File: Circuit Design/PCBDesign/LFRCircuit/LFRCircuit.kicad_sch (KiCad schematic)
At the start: 13 parts, among them M1 Motor_DC, M2 Motor_DC, U1 L293D

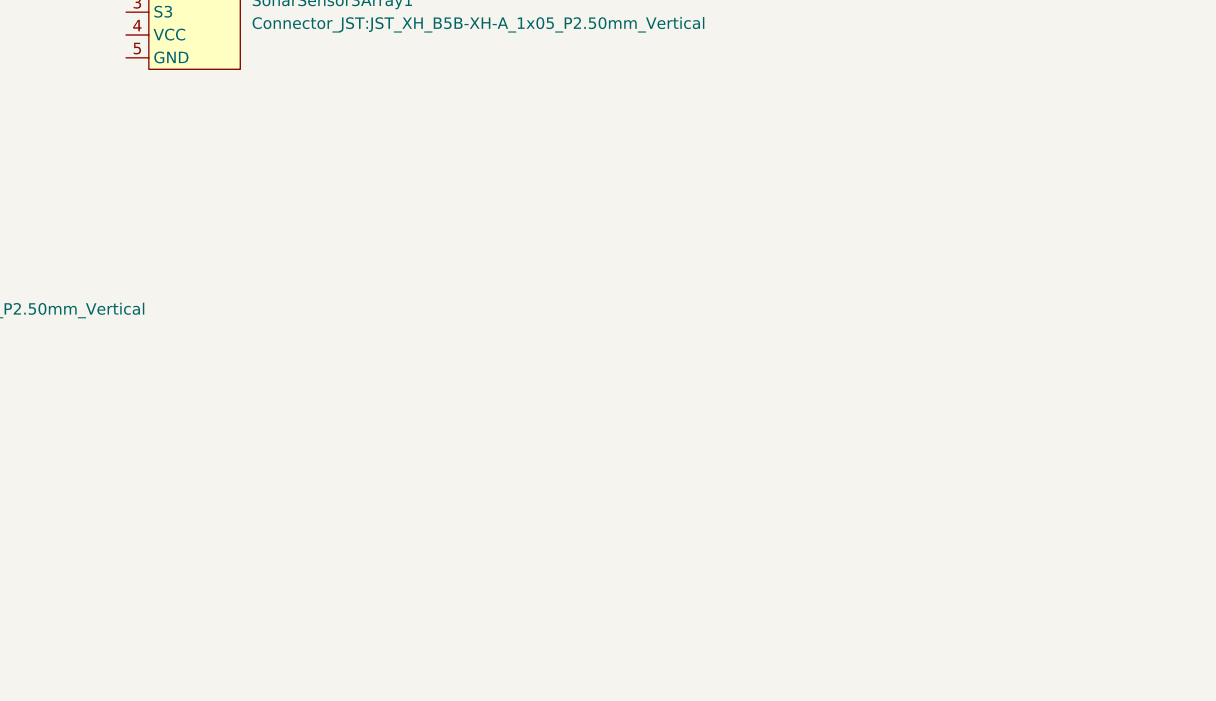
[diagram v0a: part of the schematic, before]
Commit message: Added Rotary Encoder and OLED Display Schematic
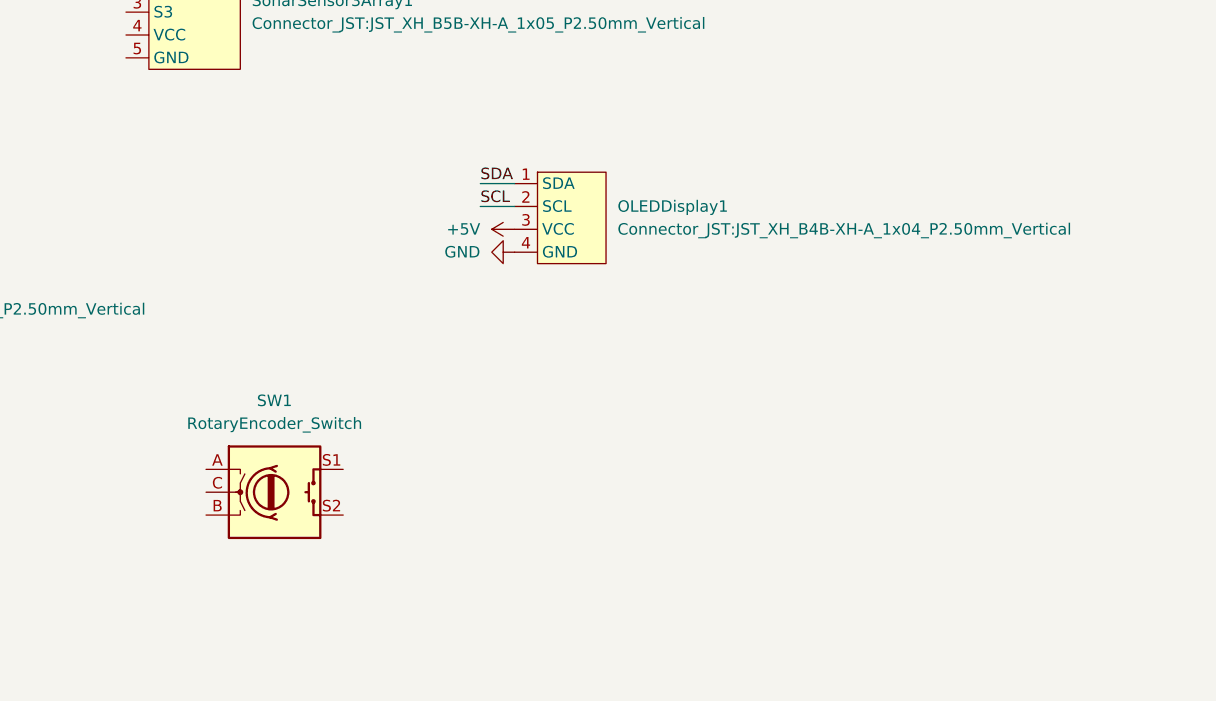
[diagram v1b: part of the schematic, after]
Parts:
- added OLEDDisplay1: ~, Connector_JST:JST_XH_B4B-XH-A_1x04_P2.50mm_Vertical, symbol LFRSymbolLib:SH1106_OLEDDisplay
- added SW1: RotaryEncoder_Switch, symbol Device:RotaryEncoder_Switch
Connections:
- net +5V: now also OLEDDisplay1.3 (VCC)
- net GND: now also OLEDDisplay1.4 (GND)
- net SCL: now also OLEDDisplay1.2 (SCL)
- net SDA: now also OLEDDisplay1.1 (SDA)

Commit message: Finalized the Schematics
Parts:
- removed SW1: RotaryEncoder_Switch, symbol Device:RotaryEncoder_Switch
- added BMSModule1: ~, Connector_JST:JST_XH_B2B-XH-A_1x02_P2.50mm_Vertical, symbol LFRSymbolLib:BMSModule
- added C3: 10uF, symbol Device:C
- added C4, C5: 0.1uF, symbol Device:C
- added C6, C7: 22uF, symbol Device:C
- added C8: 75pF, symbol Device:C
- added D5: D, symbol Device:D
- added L1: 15uH, symbol Device:L
- added R1: 49.9, symbol Device:R
- added R2: 100K, symbol Device:R
- added R3: 13.3K, symbol Device:R
- added R4: 511K, symbol Device:R
- added R5: 105K, symbol Device:R
- added RotaryEncoder1: ~, Connector_JST:JST_XH_B5B-XH-A_1x05_P2.50mm_Vertical, symbol LFRSymbolLib:RotaryEncoder
- added U2: TPS54202DDC, Package_TO_SOT_SMD:SOT-23-6, symbol Regulator_Switching:TPS54202DDC
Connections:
- net +12V: now also BMSModule1.1 (12V), C3.1, C4.1, D5.2 (A), R4.1, U2.3 (VIN)
- net +5V: now also INA1.8 (VCC), SonarSensor3Array1.4 (VCC), C6.1, C7.1, L1.2, R1.1, RotaryEncoder1.4 (+)
- net GND: now also ArduinoNanoTypeC1.4 (GND), SonarSensor3Array1.5 (GND), BMSModule1.2 (GND), C3.2, C4.2, C6.2, C7.2, C8.2, D5.1 (K), R3.2, R5.2, RotaryEncoder1.5 (GND), U2.1 (GND), U2.4 (FB)
- net 12Vout: now reaches INA1.2 (IN-), INA1.3 (VBS)
- net Alert: now reaches INA1.4 (ALE)
- net Alert: now also ArduinoNanoTypeC1.5 (D2)
- net S1: now reaches SonarSensor3Array1.1 (S1)
- net S1: now also ArduinoNanoTypeC1.7 (D4)
- net S2: now reaches SonarSensor3Array1.2 (S2)
- net S2: now also ArduinoNanoTypeC1.10 (D7)
- net S3: now reaches SonarSensor3Array1.3 (S3)
- net S3: now also ArduinoNanoTypeC1.11 (D8)
- net RE_CLK: now reaches ArduinoNanoTypeC1.13 (D10~)
- net RE_CLK: now also RotaryEncoder1.1 (CLK)
- net RE_DT: now reaches ArduinoNanoTypeC1.14 (D11~)
- net RE_DT: now also RotaryEncoder1.2 (DT)
- net RE_SW: now reaches ArduinoNanoTypeC1.15 (D12)
- net RE_SW: now also RotaryEncoder1.3 (SW)
- new net: R1.2, R2.1
- new net: C8.1, R2.2, R3.1
- new net: C5.1, L1.1, U2.2 (SW)
- new net: R4.2, R5.1, U2.5 (EN)
- new net: C5.2, U2.6 (BOOT)
- no-connect marks 0 -> 8
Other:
- note added: "Buck Converter (12V -> 5V)"
- company: (none) -> Islamic University of Technology
- title: (none) -> LFR_PCB

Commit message: Placed on the PCB
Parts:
- BMSModule1: footprint Connector_JST:JST_XH_B2B-XH-A_1x02_P2.50mm_Vertical -> Connector_JST:JST_XH_S2B-XH-A_1x02_P2.50mm_Horizontal
- C3, C4, C5, C6, C7, C8: footprint (none) -> Capacitor_SMD:C_1206_3216Metric_Pad1.33x1.80mm_HandSolder
- D1, D2, D3, D4: footprint Diode_THT:D_DO-41_SOD81_P10.16mm_Horizontal -> Diode_SMD:D_1206_3216Metric_Pad1.42x1.75mm_HandSolder
- D5: footprint (none) -> Diode_SMD:D_1206_3216Metric_Pad1.42x1.75mm_HandSolder
- IRSensor6Array1: footprint Connector_JST:JST_XH_B8B-XH-A_1x08_P2.50mm_Vertical -> Connector_JST:JST_XH_S8B-XH-A_1x08_P2.50mm_Horizontal
- L1: footprint (none) -> Inductor_SMD:L_1206_3216Metric_Pad1.42x1.75mm_HandSolder
- M1, M2: footprint Connector_JST:JST_XH_B2B-XH-AM_1x02_P2.50mm_Vertical -> Connector_JST:JST_XH_S2B-XH-A-1_1x02_P2.50mm_Horizontal
- OLEDDisplay1: footprint Connector_JST:JST_XH_B4B-XH-A_1x04_P2.50mm_Vertical -> Connector_PinSocket_2.54mm:PinSocket_1x04_P2.54mm_Vertical
- R1, R2, R3, R4, R5: footprint (none) -> Resistor_SMD:R_1206_3216Metric_Pad1.30x1.75mm_HandSolder
- RotaryEncoder1: footprint Connector_JST:JST_XH_B5B-XH-A_1x05_P2.50mm_Vertical -> Connector_JST:JST_XH_S5B-XH-A-1_1x05_P2.50mm_Horizontal
- SonarSensor3Array1: footprint Connector_JST:JST_XH_B5B-XH-A_1x05_P2.50mm_Vertical -> Connector_JST:JST_XH_S5B-XH-A_1x05_P2.50mm_Horizontal
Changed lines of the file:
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@@
 			)
 		)
-		(property "Footprint" "Connector_JST:JST_XH_B2B-XH-A_1x02_P2.50mm_Vertical"
+		(property "Footprint" "Connector_JST:JST_XH_S2B-XH-A_1x02_P2.50mm_Horizontal"
 			(at 87.63 97.7899 0)
 			(effects
@@
 			)
 		)
-		(property "Footprint" ""
+		(property "Footprint" "Resistor_SMD:R_1206_3216Metric_Pad1.30x1.75mm_HandSolder"
 			(at 248.412 128.27 90)
 			(effects
@@
 			)
 		)
-		(property "Footprint" ""
+		(property "Footprint" "Capacitor_SMD:C_1206_3216Metric_Pad1.33x1.80mm_HandSolder"
 			(at 239.7252 139.7 0)
 			(effects
@@
 			)
 		)
-		(property "Footprint" "Connector_JST:JST_XH_B8B-XH-A_1x08_P2.50mm_Vertical"
+		(property "Footprint" "Connector_JST:JST_XH_S8B-XH-A_1x08_P2.50mm_Horizontal"
 			(at 104.14 68.5799 0)
 			(effects
@@
 			)
 		)
-		(property "Footprint" "Connector_JST:JST_XH_B4B-XH-A_1x04_P2.50mm_Vertical"
+		(property "Footprint" "Connector_PinSocket_2.54mm:PinSocket_1x04_P2.54mm_Vertical"
 			(at 207.01 59.6899 0)
 			(effects
@@
 			)
 		)
-		(property "Footprint" ""
+		(property "Footprint" "Diode_SMD:D_1206_3216Metric_Pad1.42x1.75mm_HandSolder"
 			(at 152.4 120.65 0)
 			(effects
@@
 			)
 		)
-		(property "Footprint" "Connector_JST:JST_XH_B2B-XH-AM_1x02_P2.50mm_Vertical"
+		(property "Footprint" "Connector_JST:JST_XH_S2B-XH-A-1_1x02_P2.50mm_Horizontal"
 			(at 85.09 141.986 0)
 			(effects
@@
 			)
 		)
-		(property "Footprint" ""
+		(property "Footprint" "Capacitor_SMD:C_1206_3216Metric_Pad1.33x1.80mm_HandSolder"
 			(at 228.2952 124.46 0)
 			(effects
@@
 			)
 		)
-		(property "Footprint" ""
+		(property "Footprint" "Resistor_SMD:R_1206_3216Metric_Pad1.30x1.75mm_HandSolder"
 			(at 181.102 134.62 90)
 			(effects
@@
 			)
 		)
-		(property "Footprint" "Diode_THT:D_DO-41_SOD81_P10.16mm_Horizontal"
+		(property "Footprint" "Diode_SMD:D_1206_3216Metric_Pad1.42x1.75mm_HandSolder"
 			(at 101.6 137.16 0)
 			(effects
@@
 			)
 		)
-		(property "Footprint" ""
+		(property "Footprint" "Capacitor_SMD:C_1206_3216Metric_Pad1.33x1.80mm_HandSolder"
 			(at 239.7252 124.46 0)
 			(effects
@@
 			)
 		)
-		(property "Footprint" "Connector_JST:JST_XH_B5B-XH-A_1x05_P2.50mm_Vertical"
+		(property "Footprint" "Connector_JST:JST_XH_S5B-XH-A_1x05_P2.50mm_Horizontal"
 			(at 166.37 36.8299 0)
 			(effects
@@
 			)
 		)
-		(property "Footprint" "Diode_THT:D_DO-41_SOD81_P10.16mm_Horizontal"
+		(property "Footprint" "Diode_SMD:D_1206_3216Metric_Pad1.42x1.75mm_HandSolder"
 			(at 101.6 144.78 0)
 			(effects
@@
 			)
 		)
-		(property "Footprint" "Connector_JST:JST_XH_B5B-XH-A_1x05_P2.50mm_Vertical"
+		(property "Footprint" "Connector_JST:JST_XH_S5B-XH-A-1_1x05_P2.50mm_Horizontal"
 			(at 190.5 85.0899 0)
 			(effects
@@
 			)
 		)
-		(property "Footprint" ""
+		(property "Footprint" "Resistor_SMD:R_1206_3216Metric_Pad1.30x1.75mm_HandSolder"
 			(at 181.102 121.92 90)
 			(effects
@@
 			)
 		)
-		(property "Footprint" ""
+		(property "Footprint" "Resistor_SMD:R_1206_3216Metric_Pad1.30x1.75mm_HandSolder"
 			(at 248.412 135.89 90)
 			(effects
@@
 			)
 		)
-		(property "Footprint" "Diode_THT:D_DO-41_SOD81_P10.16mm_Horizontal"
+		(property "Footprint" "Diode_SMD:D_1206_3216Metric_Pad1.42x1.75mm_HandSolder"
 			(at 101.6 160.02 0)
 			(effects
@@
 			)
 		)
-		(property "Footprint" ""
+		(property "Footprint" "Capacitor_SMD:C_1206_3216Metric_Pad1.33x1.80mm_HandSolder"
 			(at 160.9852 125.73 0)
 			(effects
@@
 			)
 		)
-		(property "Footprint" "Connector_JST:JST_XH_B2B-XH-AM_1x02_P2.50mm_Vertical"
+		(property "Footprint" "Connector_JST:JST_XH_S2B-XH-A-1_1x02_P2.50mm_Horizontal"
 			(at 85.09 157.226 0)
 			(effects
@@
 			)
 		)
-		(property "Footprint" ""
+		(property "Footprint" "Inductor_SMD:L_1206_3216Metric_Pad1.42x1.75mm_HandSolder"
 			(at 223.52 116.84 0)
 			(effects
@@
 			)
 		)
-		(property "Footprint" "Diode_THT:D_DO-41_SOD81_P10.16mm_Horizontal"
+		(property "Footprint" "Diode_SMD:D_1206_3216Metric_Pad1.42x1.75mm_HandSolder"
 			(at 101.6 152.4 0)
 			(effects
@@
 			)
 		)
-		(property "Footprint" ""
+		(property "Footprint" "Capacitor_SMD:C_1206_3216Metric_Pad1.33x1.80mm_HandSolder"
 			(at 212.09 117.8052 0)
 			(effects
@@
 			)
 		)
-		(property "Footprint" ""
+		(property "Footprint" "Capacitor_SMD:C_1206_3216Metric_Pad1.33x1.80mm_HandSolder"
 			(at 172.4152 125.73 0)
 			(effects
@@
 			)
 		)
-		(property "Footprint" ""
+		(property "Footprint" "Resistor_SMD:R_1206_3216Metric_Pad1.30x1.75mm_HandSolder"
 			(at 248.412 120.65 90)
 			(effects
